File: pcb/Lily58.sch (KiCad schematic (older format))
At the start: 128 parts, among them J2 4PIN, J3 Conn_01x06_Female, J4 Conn_01x06_Female, P1 i2c_pin, P2 i2c_pin, SW1 SW_PUSH, SW10 SW_PUSH, SW11 SW_PUSH, SW12 SW_PUSH, SW13 SW_PUSH, SW14 SW_PUSH, SW15 SW_PUSH, SW16 SW_PUSH, SW17 SW_PUSH, SW18 SW_PUSH, SW19 SW_PUSH, SW2 SW_PUSH, SW20 SW_PUSH, SW21 SW_PUSH, SW22 SW_PUSH, SW23 SW_PUSH, SW24 SW_PUSH, SW25 SW_PUSH, SW26 SW_PUSH, SW27 SW_PUSH, SW28 SW_PUSH, SW29 SW_PUSH, SW3 SW_PUSH, SW4 SW_PUSH, SW5 SW_PUSH, SW6 SW_PUSH, SW7 SW_PUSH, SW8 SW_PUSH, SW9 SW_PUSH, U1 ProMicro

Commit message: update pcb
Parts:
- removed P1, P2: i2c_pin, Lily58-footprint:1pin_conn, symbol Lily58-rescue:i2c_pin-Lily58-cache
- removed W1: jumper, Lily58-footprint:jumper_data, symbol Device:Jumper
- added JP21: 1S, Lily58-footprint:Jumper, symbol Device:Jumper_NO_Small
- added JP22: I2C, Lily58-footprint:Jumper, symbol Device:Jumper_NO_Small
- TH3, TH4, TH5, TH6, TH7: footprint Lily58-footprint:HOLE_M2_TH -> Lily58-footprint:HOLE_M2
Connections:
- net DATA: now also JP20.2, JP9.2, JP21.2
- net GND: now also J2.3; no longer J2.2
- net SCL: now also JP22.2
- net SDA: now also J2.2
- net VCC: now also J2.4; no longer J2.1, JP20.2, JP9.2
- net D4: now reaches LED1.2 (A), U1.7 (D4(PD4))
- new net: J2.1, JP21.1, JP22.1
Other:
- moved on the sheet: R1, R2
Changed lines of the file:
@@
 L Lily58-rescue:VCC-Lily58-cache #PWR05
 U 1 1 5B739B47
-P 4400 4800
-F 0 "#PWR05" H 4400 4650 50  0001 C CNN
-F 1 "VCC" H 4400 4950 50  0000 C CNN
-F 2 "" H 4400 4800 50  0001 C CNN
-F 3 "" H 4400 4800 50  0001 C CNN
-	1    4400 4800
+P 2300 5000
+F 0 "#PWR05" H 2300 4850 50  0001 C CNN
+F 1 "VCC" H 2300 5150 50  0000 C CNN
+F 2 "" H 2300 5000 50  0001 C CNN
+F 3 "" H 2300 5000 50  0001 C CNN
+	1    2300 5000
 	1    0    0    -1
 $EndComp
@@
 L Lily58-rescue:VCC-Lily58-cache #PWR06
 U 1 1 5B739CDC
-P 4550 4800
-F 0 "#PWR06" H 4550 4650 50  0001 C CNN
-F 1 "VCC" H 4550 4950 50  0000 C CNN
-F 2 "" H 4550 4800 50  0001 C CNN
-F 3 "" H 4550 4800 50  0001 C CNN
-	1    4550 4800
+P 2450 5000
+F 0 "#PWR06" H 2450 4850 50  0001 C CNN
+F 1 "VCC" H 2450 5150 50  0000 C CNN
+F 2 "" H 2450 5000 50  0001 C CNN
+F 3 "" H 2450 5000 50  0001 C CNN
+	1    2450 5000
 	1    0    0    -1
 $EndComp
@@
 L Lily58-rescue:R-Lily58-cache R1
 U 1 1 5B739F4A
-P 4400 4950
-F 0 "R1" V 4500 4950 50  0000 C BNN
-F 1 "R" V 4400 4950 50  0000 C CNN
-F 2 "Lily58-footprint:RESISTOR_mini" V 4330 4950 50  0001 C CNN
-F 3 "" H 4400 4950 50  0001 C CNN
-	1    4400 4950
+P 2300 5150
+F 0 "R1" V 2400 5150 50  0000 C BNN
+F 1 "R" V 2300 5150 50  0000 C CNN
+F 2 "Lily58-footprint:RESISTOR_mini" V 2230 5150 50  0001 C CNN
+F 3 "" H 2300 5150 50  0001 C CNN
+	1    2300 5150
 	1    0    0    -1
 $EndComp
@@
 L Lily58-rescue:R-Lily58-cache R2
 U 1 1 5B73A034
-P 4550 4950
-F 0 "R2" V 4650 4950 50  0000 C BNN
-F 1 "R" V 4550 4950 50  0000 C CNN
-F 2 "Lily58-footprint:RESISTOR_mini" V 4480 4950 50  0001 C CNN
-F 3 "" H 4550 4950 50  0001 C CNN
-	1    4550 4950
-	1    0    0    -1
-$EndComp
-Text GLabel 4400 5100 3    50   Input ~ 0
+P 2450 5150
+F 0 "R2" V 2550 5150 50  0000 C BNN
+F 1 "R" V 2450 5150 50  0000 C CNN
+F 2 "Lily58-footprint:RESISTOR_mini" V 2380 5150 50  0001 C CNN
+F 3 "" H 2450 5150 50  0001 C CNN
+	1    2450 5150
+	1    0    0    -1
+$EndComp
+Text GLabel 2300 5300 3    50   Input ~ 0
 SDA
 $Comp
@@
 	1    0    0    -1
 $EndComp
-$Comp
-L Lily58-rescue:HOLE-Lily58-cache TH4
-U 1 1 5B74D1C0
-P 8450 6150
-F 0 "TH4" H 8450 6150 60  0000 C CNN
-F 1 "HOLE" H 8450 6050 60  0000 C CNN
-F 2 "Lily58-footprint:HOLE_M2_TH" H 8450 6150 60  0001 C CNN
-F 3 "" H 8450 6150 60  0000 C CNN
-	1    8450 6150
-	1    0    0    -1
-$EndComp
-$Comp
-L Lily58-rescue:HOLE-Lily58-cache TH5
-U 1 1 5B74D78B
-P 8800 6150
-F 0 "TH5" H 8800 6150 60  0000 C CNN
-F 1 "HOLE" H 8800 6050 60  0000 C CNN
-F 2 "Lily58-footprint:HOLE_M2_TH" H 8800 6150 60  0001 C CNN
-F 3 "" H 8800 6150 60  0000 C CNN
-	1    8800 6150
-	1    0    0    -1
-$EndComp
-$Comp
-L Lily58-rescue:HOLE-Lily58-cache TH6
-U 1 1 5B74D88C
-P 9150 6150
-F 0 "TH6" H 9150 6150 60  0000 C CNN
-F 1 "HOLE" H 9150 6050 60  0000 C CNN
-F 2 "Lily58-footprint:HOLE_M2_TH" H 9150 6150 60  0001 C CNN
-F 3 "" H 9150 6150 60  0000 C CNN
-	1    9150 6150
-	1    0    0    -1
-$EndComp
-$Comp
-L Lily58-rescue:HOLE-Lily58-cache TH7
-U 1 1 5B74D98F
-P 9500 6150
-F 0 "TH7" H 9500 6150 60  0000 C CNN
-F 1 "HOLE" H 9500 6050 60  0000 C CNN
-F 2 "Lily58-footprint:HOLE_M2_TH" H 9500 6150 60  0001 C CNN
-F 3 "" H 9500 6150 60  0000 C CNN
-	1    9500 6150
-	1    0    0    -1
-$EndComp
-$Comp
-L Lily58-rescue:HOLE-Lily58-cache TH3
-U 1 1 5B74DA95
-P 8100 6150
-F 0 "TH3" H 8100 6150 60  0000 C CNN
-F 1 "HOLE" H 8100 6050 60  0000 C CNN
-F 2 "Lily58-footprint:HOLE_M2_TH" H 8100 6150 60  0001 C CNN
-F 3 "" H 8100 6150 60  0000 C CNN
-	1    8100 6150
-	1    0    0    -1
-$EndComp
-Text GLabel 4550 5100 3    50   Input ~ 0
+Text GLabel 2450 5300 3    50   Input ~ 0
 SCL
 Connection ~ 7700 2550
@@
 	1    0    0    -1
 $EndComp
-Wire Wire Line
-	3250 4350 3150 4350
-Wire Wire Line
-	3150 4450 3250 4450
-$Comp
-L Lily58-rescue:i2c_pin-Lily58-cache P1
-U 1 1 5B8F6780
-P 3550 4000
-F 0 "P1" H 3550 4100 50  0000 C CNN
-F 1 "i2c_pin" V 3650 4000 50  0000 C CNN
-F 2 "Lily58-footprint:1pin_conn" H 3550 4000 50  0001 C CNN
-F 3 "" H 3550 4000 50  0001 C CNN
-	1    3550 4000
-	0    -1   -1   0
-$EndComp
-$Comp
-L Lily58-rescue:i2c_pin-Lily58-cache P2
-U 1 1 5B8F6980
-P 3550 4750
-F 0 "P2" H 3550 4650 50  0000 C CNN
-F 1 "i2c_pin" V 3650 4750 50  0000 C CNN
-F 2 "Lily58-footprint:1pin_conn" H 3550 4750 50  0001 C CNN
-F 3 "" H 3550 4750 50  0001 C CNN
-	1    3550 4750
-	0    1    1    0
-$EndComp
-Wire Wire Line
-	3150 4550 3550 4550
-Wire Wire Line
-	3150 4200 3550 4200
-Wire Wire Line
-	3250 4150 3250 4350
-Wire Wire Line
-	3250 4450 3250 4600
-$Comp
-L Device:Jumper W1
-U 1 1 5B900157
-P 3850 4550
-F 0 "W1" H 3850 4500 50  0000 C CNN
-F 1 "jumper" H 3850 4700 50  0000 C CNN
-F 2 "Lily58-footprint:jumper_data" H 3850 4550 50  0001 C CNN
-F 3 "" H 3850 4550 50  0000 C CNN
-	1    3850 4550
-	-1   0    0    1
-$EndComp
 Text GLabel 2550 2200 0    50   Input ~ 0
 DATA
-Text GLabel 4150 4550 2    50   Input ~ 0
+Text GLabel 3850 4250 2    50   Input ~ 0
 DATA
-Connection ~ 3550 4550
 Text Label 3850 3000 0    50   ~ 0
 MISO
@@
 	0    -1   -1   0
 $EndComp
-$Comp
-L power:VCC #PWR0115
-U 1 1 61C44B56
-P 3050 7000
-F 0 "#PWR0115" H 3050 6850 50  0001 C CNN
-F 1 "VCC" V 3050 7150 50  0000 L CNN
-F 2 "" H 3050 7000 50  0001 C CNN
-F 3 "" H 3050 7000 50  0001 C CNN
-	1    3050 7000
-	0    1    1    0
-$EndComp
 Text GLabel 3050 7400 2    50   Input ~ 0
 A2
 Text GLabel 3050 7100 2    50   Input ~ 0
 A3
-$Comp
-L power:VCC #PWR0116
-U 1 1 61C4BDD2
-P 3050 8200
-F 0 "#PWR0116" H 3050 8050 50  0001 C CNN
-F 1 "VCC" V 3050 8350 50  0000 L CNN
-F 2 "" H 3050 8200 50  0001 C CNN
-F 3 "" H 3050 8200 50  0001 C CNN
-	1    3050 8200
-	0    1    1    0
-$EndComp
 Text GLabel 3050 8100 2    50   Input ~ 0
 A3
@@
 Text GLabel 9500 2250 1    50   Input ~ 0
 col0
-Text GLabel 3050 7300 2    50   Input ~ 0
-col0
-Text GLabel 3050 7500 2    50   Input ~ 0
-row4
-Text GLabel 3050 7900 2    50   Input ~ 0
-col0
-Text GLabel 3050 7700 2    50   Input ~ 0
-row4
 Wire Wire Line
 	2350 7400 2600 7400
@@
 	1    0    0    -1
 $EndComp
+Text GLabel 1650 2700 0    50   Input ~ 0
+D4
+Wire Wire Line
+	1650 2700 1850 2700
+Text GLabel 3050 7700 2    50   Input ~ 0
+row4
+Text GLabel 3050 7900 2    50   Input ~ 0
+col0
+Text GLabel 3050 7500 2    50   Input ~ 0
+row4
+Text GLabel 3050 7300 2    50   Input ~ 0
+col0
+Text GLabel 3050 7000 2    50   Input ~ 0
+DATA
+Text GLabel 3050 8200 2    50   Input ~ 0
+DATA
+$Comp
+L Device:Jumper_NO_Small JP21
+U 1 1 61E99623
+P 3750 4250
+F 0 "JP21" H 3750 4200 50  0000 C CNN
+F 1 "1S" H 3750 4344 50  0001 C CNN
+F 2 "Lily58-footprint:Jumper" H 3750 4250 50  0001 C CNN
+F 3 "~" H 3750 4250 50  0001 C CNN
+	1    3750 4250
+	1    0    0    -1
+$EndComp
+$Comp
+L Device:Jumper_NO_Small JP22
+U 1 1 61E9BC56
+P 3750 4450
+F 0 "JP22" H 3750 4400 50  0000 C CNN
+F 1 "I2C" H 3750 4544 50  0001 C CNN
+F 2 "Lily58-footprint:Jumper" H 3750 4450 50  0001 C CNN
+F 3 "~" H 3750 4450 50  0001 C CNN
+	1    3750 4450
+	1    0    0    -1
+$EndComp
+Text GLabel 3350 4450 2    50   Input ~ 0
+SDA
+Text GLabel 3850 4450 2    50   Input ~ 0
+SCL
+Wire Wire Line
+	3150 4200 3250 4200
+Wire Wire Line
+	3250 4200 3250 4150
+Wire Wire Line
+	3150 4450 3350 4450
+Wire Wire Line
+	3650 4250 3650 4350
+Wire Wire Line
+	3150 4550 3250 4550
+Wire Wire Line
+	3250 4550 3250 4600
+Wire Wire Line
+	3150 4350 3650 4350
+Connection ~ 3650 4350
+Wire Wire Line
+	3650 4350 3650 4450
+$Comp
+L Lily58-rescue:HOLE-Lily58-cache TH3
+U 1 1 5B74DA95
+P 8100 6150
+F 0 "TH3" H 8100 6150 60  0000 C CNN
+F 1 "HOLE" H 8100 6050 60  0000 C CNN
+F 2 "Lily58-footprint:HOLE_M2" H 8100 6150 60  0001 C CNN
+F 3 "" H 8100 6150 60  0000 C CNN
+	1    8100 6150
+	1    0    0    -1
+$EndComp
+$Comp
+L Lily58-rescue:HOLE-Lily58-cache TH7
+U 1 1 5B74D98F
+P 9500 6150
+F 0 "TH7" H 9500 6150 60  0000 C CNN
+F 1 "HOLE" H 9500 6050 60  0000 C CNN
+F 2 "Lily58-footprint:HOLE_M2" H 9500 6150 60  0001 C CNN
+F 3 "" H 9500 6150 60  0000 C CNN
+	1    9500 6150
+	1    0    0    -1
+$EndComp
+$Comp
+L Lily58-rescue:HOLE-Lily58-cache TH6
+U 1 1 5B74D88C
+P 9150 6150
+F 0 "TH6" H 9150 6150 60  0000 C CNN
+F 1 "HOLE" H 9150 6050 60  0000 C CNN
+F 2 "Lily58-footprint:HOLE_M2" H 9150 6150 60  0001 C CNN
+F 3 "" H 9150 6150 60  0000 C CNN
+	1    9150 6150
+	1    0    0    -1
+$EndComp
+$Comp
+L Lily58-rescue:HOLE-Lily58-cache TH5
+U 1 1 5B74D78B
+P 8800 6150
+F 0 "TH5" H 8800 6150 60  0000 C CNN
+F 1 "HOLE" H 8800 6050 60  0000 C CNN
+F 2 "Lily58-footprint:HOLE_M2" H 8800 6150 60  0001 C CNN
+F 3 "" H 8800 6150 60  0000 C CNN
+	1    8800 6150
+	1    0    0    -1
+$EndComp
+$Comp
+L Lily58-rescue:HOLE-Lily58-cache TH4
+U 1 1 5B74D1C0
+P 8450 6150
+F 0 "TH4" H 8450 6150 60  0000 C CNN
+F 1 "HOLE" H 8450 6050 60  0000 C CNN
+F 2 "Lily58-footprint:HOLE_M2" H 8450 6150 60  0001 C CNN
+F 3 "" H 8450 6150 60  0000 C CNN
+	1    8450 6150
+	1    0    0    -1
+$EndComp

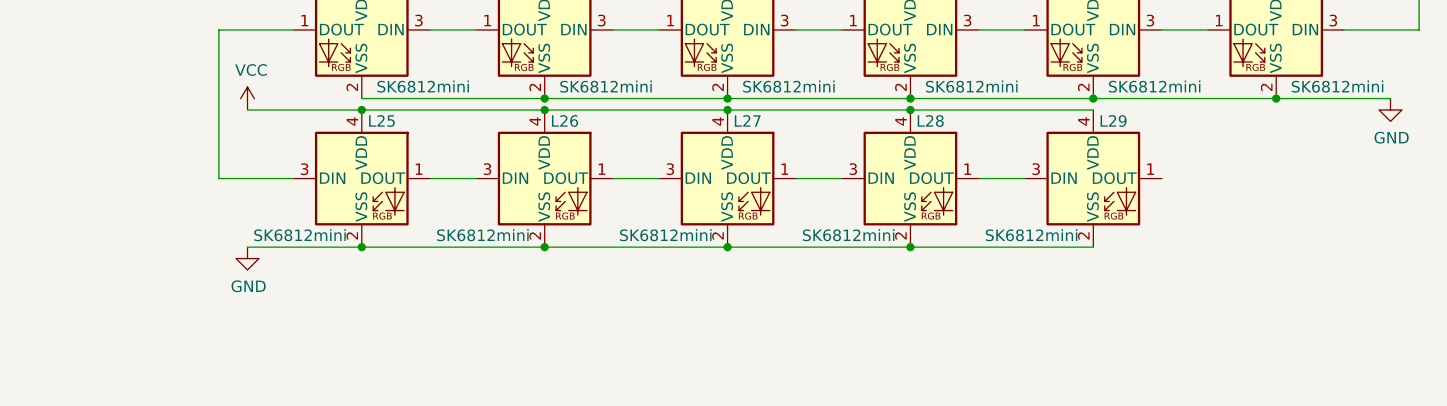
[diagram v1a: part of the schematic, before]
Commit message: add underglow
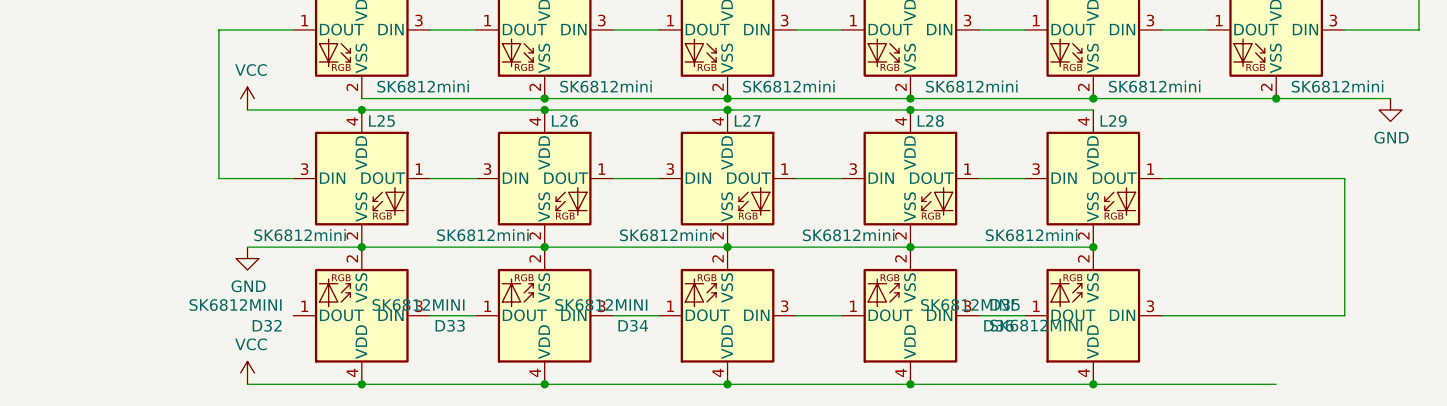
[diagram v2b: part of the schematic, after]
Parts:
- added D32, D33, D34, D35, D36: SK6812MINI, Lily58-footprint:SK6812MINI_underglow_rev, symbol LED:SK6812MINI
- D1, D10, D11, D12, D13, D14, D15, D16, D17, D18, D19, D2, D20, D21, D22, D23, D24, D25, D26, D27, D28, D29, D3, D4, D5, D6, D7, D8, D9: footprint Lily58-footprint:Diode_TH_SOD123 -> Lily58-footprint:Diode_SOD123
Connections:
- net GND: now also D32.2 (VSS), D33.2 (VSS), D34.2 (VSS), D35.2 (VSS), D36.2 (VSS)
- net VCC: now also D32.4 (VDD), D33.4 (VDD), D34.4 (VDD), D35.4 (VDD), D36.4 (VDD)
- net at L29.1 (DOUT): now also D36.3 (DIN)
- new net: D34.3 (DIN), D35.1 (DOUT)
- new net: D35.3 (DIN), D36.1 (DOUT)
- new net: D33.3 (DIN), D34.1 (DOUT)
- new net: D32.3 (DIN), D33.1 (DOUT)

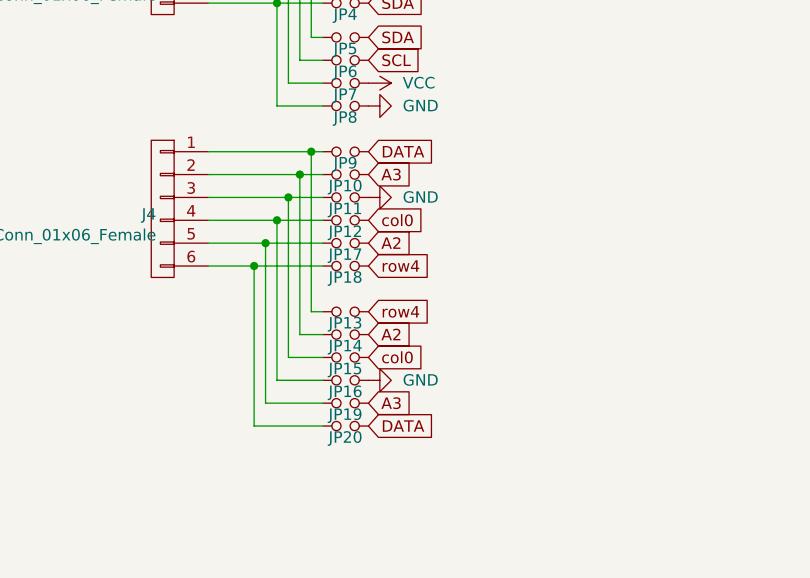
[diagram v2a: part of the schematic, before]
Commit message: fix joystick pinout
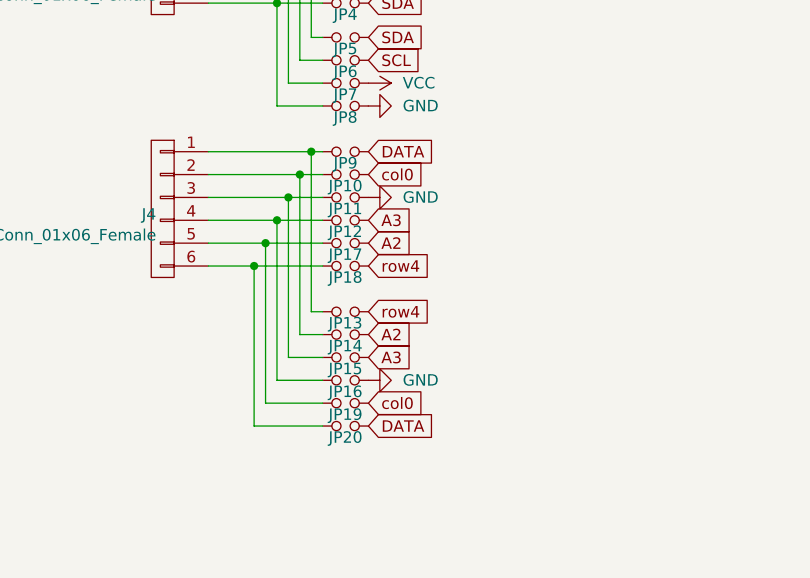
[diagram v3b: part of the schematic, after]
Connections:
- net A3: now also JP12.2, JP15.2; no longer JP10.2, JP19.2
- net col0: now also JP10.2, JP19.2; no longer JP12.2, JP15.2
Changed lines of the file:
@@
 Text GLabel 3050 7400 2    50   Input ~ 0
 A2
-Text GLabel 3050 7100 2    50   Input ~ 0
+Text GLabel 3050 7300 2    50   Input ~ 0
 A3
-Text GLabel 3050 8100 2    50   Input ~ 0
+Text GLabel 3050 7900 2    50   Input ~ 0
 A3
 Text GLabel 3050 7800 2    50   Input ~ 0
@@
 Text GLabel 3050 7700 2    50   Input ~ 0
 row4
-Text GLabel 3050 7900 2    50   Input ~ 0
+Text GLabel 3050 8100 2    50   Input ~ 0
 col0
 Text GLabel 3050 7500 2    50   Input ~ 0
 row4
-Text GLabel 3050 7300 2    50   Input ~ 0
+Text GLabel 3050 7100 2    50   Input ~ 0
 col0
 Text GLabel 3050 7000 2    50   Input ~ 0
